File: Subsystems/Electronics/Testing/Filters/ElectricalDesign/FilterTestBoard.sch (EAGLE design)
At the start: 0 parts

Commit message: Created Schematic for Filter Test Board
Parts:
- added C1, C2, C3, C4: 1nF 10%, CougsInSpace-Capacitors:CAP-V-1NF-1608
- added C5, C6, C7, C8: 1nF 10%, CougsInSpace-Capacitors:CAP-H-1NF-1608
- added J1, J2: (no value), CougsInSpace-Connectors:COAX-BNC-T-R
- added R1, R2, R3, R4: 0Ω <20mΩ, CougsInSpace-Resistors:RES-H-0-1608
- added R5, R6, R7, R8: 0Ω <20mΩ, CougsInSpace-Resistors:RES-V-0-1608
- added SW1, SW2, SW3: (no value), CougsInSpace-Switches:SWITCH-DPDT-100DP1T1B1M2QE
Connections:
- new net N$1: C1.1, R1.2, R2.1
- new net N$10: C4.1, C7.1, R4.2
- new net N$11: R1.1, SW1.1-B
- new net N$12: C6.2, R6.2, SW3.1-A
- new net N$13: C5.2, C6.1, R5.2
- new net N$14: J1.CENTER, SW1.COM-A, SW2.COM-A, SW3.COM-A
- new net N$15: J2.CENTER, SW1.COM-B, SW2.COM-B, SW3.COM-B
- new net N$2: C2.1, R2.2, SW1.1-A
- new net N$3: C8.2, R8.2, SW2.1-A
- new net N$4: C5.1, SW3.1-B
- new net N$7: C7.2, C8.1, R7.2
- new net N$8: C3.1, R3.2, R4.1
- new net N$9: R3.1, SW2.1-B
- new net PGND: C1.2, C2.2, C3.2, C4.2, J1.SHIELD, J2.SHIELD, R5.1, R6.1, R7.1, R8.1
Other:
- note added: "Band Pass Filter"
- note added: "Connector: Input 50Ω"
- note added: "Connector: Output 1MΩ"
- note added: "High Pass Filter"
- note added: "Low Pass Filter"
- note added: "Page 1: Block Diagram Page 2: Filters, Connectors"
- note added: "Switch"
- note removed: "Connector: From Board"

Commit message: Laid out Board
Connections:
- net N$1 renamed LOW_INT
- net N$10 renamed BAND_INT1
- net N$11 renamed LOW_IN
- net N$12 renamed HIGH_OUT
- net N$13 renamed HIGH_INT
- net N$14 renamed INPUT
- net N$15 renamed OUTPUT
- net N$2 renamed LOW_OUT
- net N$3 renamed BAND_OUT
- net N$4 renamed HIGH_IN
- net N$7 renamed BAND_INT2
- net N$8 renamed BAND_INT0
- net N$9 renamed BAND_IN
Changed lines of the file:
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@@
 </attributes>
 <variantdefs>
+<variantdef name="EPS Test"/>
 </variantdefs>
 <classes>
@@
 </busses>
 <nets>
-<net name="N$1" class="0">
+<net name="LOW_INT" class="0">
 <segment>
 <pinref part="R1" gate="G$1" pin="2"/>
@@
 </segment>
 </net>
-<net name="N$2" class="0">
+<net name="LOW_OUT" class="0">
 <segment>
 <pinref part="R2" gate="G$1" pin="2"/>
@@
 </segment>
 </net>
-<net name="N$8" class="0">
+<net name="BAND_INT0" class="0">
 <segment>
 <pinref part="R3" gate="G$1" pin="2"/>
@@
 </segment>
 </net>
-<net name="N$12" class="0">
+<net name="HIGH_OUT" class="0">
 <segment>
 <pinref part="C6" gate="G$1" pin="2"/>
@@
 </segment>
 </net>
-<net name="N$13" class="0">
+<net name="HIGH_INT" class="0">
 <segment>
 <pinref part="C6" gate="G$1" pin="1"/>
@@
 </segment>
 </net>
-<net name="N$3" class="0">
+<net name="BAND_OUT" class="0">
 <segment>
 <pinref part="C8" gate="G$1" pin="2"/>
@@
 </segment>
 </net>
-<net name="N$7" class="0">
+<net name="BAND_INT2" class="0">
 <segment>
 <pinref part="C8" gate="G$1" pin="1"/>
@@
 </segment>
 </net>
-<net name="N$10" class="0">
+<net name="BAND_INT1" class="0">
 <segment>
 <pinref part="C7" gate="G$1" pin="1"/>
@@
 </segment>
 </net>
-<net name="N$4" class="0">
+<net name="HIGH_IN" class="0">
 <segment>
 <pinref part="C5" gate="G$1" pin="1"/>
@@
 </segment>
 </net>
-<net name="N$9" class="0">
+<net name="BAND_IN" class="0">
 <segment>
 <pinref part="R3" gate="G$1" pin="1"/>
@@
 </segment>
 </net>
-<net name="N$11" class="0">
+<net name="LOW_IN" class="0">
 <segment>
 <pinref part="R1" gate="G$1" pin="1"/>
@@
 </segment>
 </net>
-<net name="N$14" class="0">
+<net name="INPUT" class="0">
 <segment>
 <pinref part="J1" gate="G$1" pin="CENTER"/>
@@
 </segment>
 </net>
-<net name="N$15" class="0">
+<net name="OUTPUT" class="0">
 <segment>
 <pinref part="J2" gate="G$1" pin="CENTER"/>

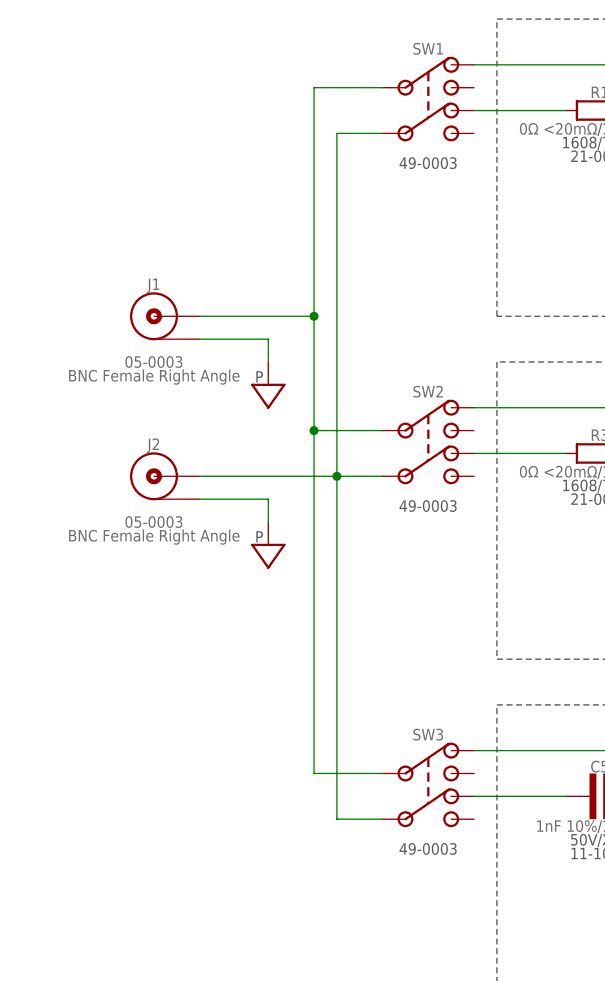
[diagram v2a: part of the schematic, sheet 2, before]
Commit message: Adjusted Board Layout
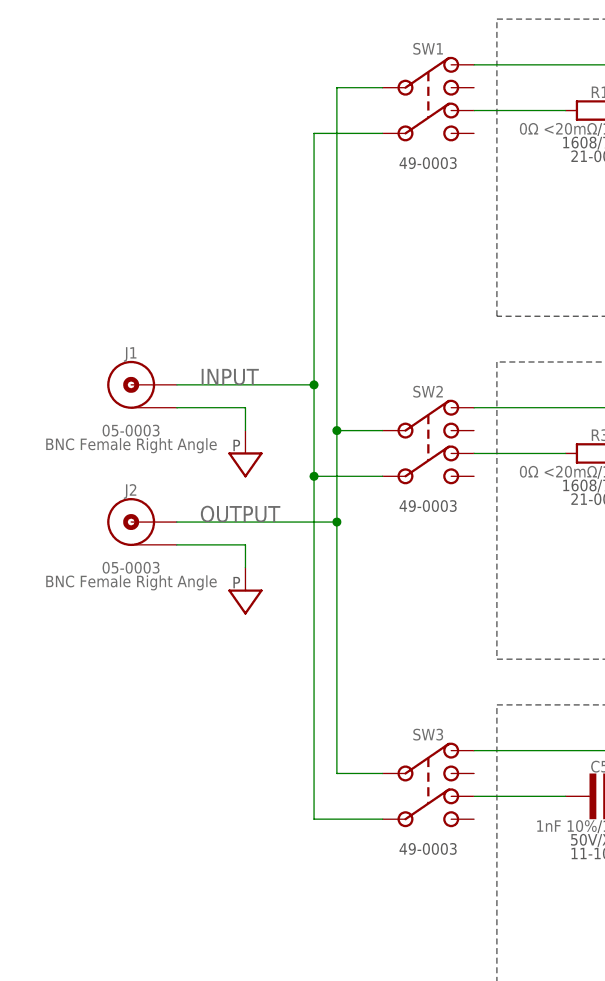
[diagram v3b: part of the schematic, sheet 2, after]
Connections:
- net INPUT: now also SW1.COM-B, SW2.COM-B, SW3.COM-B; no longer SW1.COM-A, SW2.COM-A, SW3.COM-A
- net OUTPUT: now also SW1.COM-A, SW2.COM-A, SW3.COM-A; no longer SW1.COM-B, SW2.COM-B, SW3.COM-B
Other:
- moved on the sheet: J1, J2
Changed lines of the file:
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@@
 <part name="SW2" library="CougsInSpace-Switches" deviceset="SWITCH-DPDT" device="-100DP1T1B1M2QE"/>
 <part name="SW3" library="CougsInSpace-Switches" deviceset="SWITCH-DPDT" device="-100DP1T1B1M2QE"/>
-<part name="R1" library="CougsInSpace-Resistors" deviceset="RES-H" device="-1608" technology="-0" value="0Ω &lt;20mΩ"/>
-<part name="R2" library="CougsInSpace-Resistors" deviceset="RES-H" device="-1608" technology="-0" value="0Ω &lt;20mΩ"/>
+<part name="R1" library="CougsInSpace-Resistors" deviceset="RES-H" device="-1608" technology="-0" value="0Ω &lt;20mΩ">
+<variant name="EPS Test" technology="-158K" value="158kΩ 0.1%"/>
+</part>
+<part name="R2" library="CougsInSpace-Resistors" deviceset="RES-H" device="-1608" technology="-0" value="0Ω &lt;20mΩ">
+<variant name="EPS Test" technology="-158K" value="158kΩ 0.1%"/>
+</part>
 <part name="C1" library="CougsInSpace-Capacitors" deviceset="CAP-V" device="-1608" technology="-1NF" value="1nF 10%"/>
 <part name="C2" library="CougsInSpace-Capacitors" deviceset="CAP-V" device="-1608" technology="-1NF" value="1nF 10%"/>
 <part name="J2" library="CougsInSpace-Connectors" deviceset="COAX" device="-BNC-T-R"/>
-<part name="R3" library="CougsInSpace-Resistors" deviceset="RES-H" device="-1608" technology="-0" value="0Ω &lt;20mΩ"/>
-<part name="R4" library="CougsInSpace-Resistors" deviceset="RES-H" device="-1608" technology="-0" value="0Ω &lt;20mΩ"/>
+<part name="R3" library="CougsInSpace-Resistors" deviceset="RES-H" device="-1608" technology="-0" value="0Ω &lt;20mΩ">
+<variant name="EPS Test" technology="-158K" value="158kΩ 0.1%"/>
+</part>
+<part name="R4" library="CougsInSpace-Resistors" deviceset="RES-H" device="-1608" technology="-0" value="0Ω &lt;20mΩ">
+<variant name="EPS Test" technology="-158K" value="158kΩ 0.1%"/>
+</part>
 <part name="C3" library="CougsInSpace-Capacitors" deviceset="CAP-V" device="-1608" technology="-1NF" value="1nF 10%"/>
 <part name="C4" library="CougsInSpace-Capacitors" deviceset="CAP-V" device="-1608" technology="-1NF" value="1nF 10%"/>
@@
 <attribute name="TITLE" x="227.33" y="20.32" size="3.81" layer="94" ratio="15" align="bottom-right"/>
 </instance>
-<instance part="J1" gate="G$1" x="50.8" y="121.92" smashed="yes" rot="MR0">
-<attribute name="NAME" x="50.8" y="125.476" size="1.27" layer="95" rot="MR0" align="center"/>
-<attribute name="VALUE" x="50.8" y="118.364" size="1.27" layer="96" rot="MR0" align="center"/>
-<attribute name="SKU" x="50.8" y="116.84" size="1.27" layer="96" rot="MR0" align="center"/>
-<attribute name="PACKAGE" x="50.8" y="115.316" size="1.27" layer="96" rot="MR0" align="center"/>
+<instance part="J1" gate="G$1" x="48.26" y="114.3" smashed="yes" rot="MR0">
+<attribute name="NAME" x="48.26" y="117.856" size="1.27" layer="95" rot="MR0" align="center"/>
+<attribute name="VALUE" x="48.26" y="110.744" size="1.27" layer="96" rot="MR0" align="center"/>
+<attribute name="SKU" x="48.26" y="109.22" size="1.27" layer="96" rot="MR0" align="center"/>
+<attribute name="PACKAGE" x="48.26" y="107.696" size="1.27" layer="96" rot="MR0" align="center"/>
 </instance>
 <instance part="SW1" gate="G$1" x="81.28" y="144.78" smashed="yes">
@@
 <attribute name="TEMP" x="142.494" y="132.08" size="1.27" layer="97" align="center-left"/>
 </instance>
-<instance part="J2" gate="G$1" x="50.8" y="104.14" smashed="yes" rot="MR0">
-<attribute name="NAME" x="50.8" y="107.696" size="1.27" layer="95" rot="MR0" align="center"/>
-<attribute name="VALUE" x="50.8" y="100.584" size="1.27" layer="96" rot="MR0" align="center"/>
-<attribute name="SKU" x="50.8" y="99.06" size="1.27" layer="96" rot="MR0" align="center"/>
-<attribute name="PACKAGE" x="50.8" y="97.536" size="1.27" layer="96" rot="MR0" align="center"/>
+<instance part="J2" gate="G$1" x="48.26" y="99.06" smashed="yes" rot="MR0">
+<attribute name="NAME" x="48.26" y="102.616" size="1.27" layer="95" rot="MR0" align="center"/>
+<attribute name="VALUE" x="48.26" y="95.504" size="1.27" layer="96" rot="MR0" align="center"/>
+<attribute name="SKU" x="48.26" y="93.98" size="1.27" layer="96" rot="MR0" align="center"/>
+<attribute name="PACKAGE" x="48.26" y="92.456" size="1.27" layer="96" rot="MR0" align="center"/>
 </instance>
 <instance part="R3" gate="G$1" x="101.6" y="106.68" smashed="yes">
@@
 <attribute name="SKU" x="140.97" y="60.452" size="1.27" layer="97" align="center-left"/>
 </instance>
-<instance part="SUPPLY1" gate="G$1" x="63.5" y="114.3" smashed="yes"/>
-<instance part="SUPPLY2" gate="G$1" x="63.5" y="96.52" smashed="yes"/>
+<instance part="SUPPLY1" gate="G$1" x="60.96" y="106.68" smashed="yes"/>
+<instance part="SUPPLY2" gate="G$1" x="60.96" y="91.44" smashed="yes"/>
 <instance part="SUPPLY3" gate="G$1" x="139.7" y="127" smashed="yes"/>
 <instance part="SUPPLY4" gate="G$1" x="111.76" y="127" smashed="yes"/>
@@
 <segment>
 <pinref part="J1" gate="G$1" pin="SHIELD"/>
-<wire x1="55.88" y1="119.38" x2="63.5" y2="119.38" width="0.1524" layer="91"/>
+<wire x1="53.34" y1="111.76" x2="60.96" y2="111.76" width="0.1524" layer="91"/>
 <pinref part="SUPPLY1" gate="G$1" pin="PGND"/>
-<wire x1="63.5" y1="119.38" x2="63.5" y2="116.84" width="0.1524" layer="91"/>
+<wire x1="60.96" y1="111.76" x2="60.96" y2="109.22" width="0.1524" layer="91"/>
 </segment>
 <segment>
 <pinref part="J2" gate="G$1" pin="SHIELD"/>
-<wire x1="63.5" y1="101.6" x2="55.88" y2="101.6" width="0.1524" layer="91"/>
+<wire x1="60.96" y1="96.52" x2="53.34" y2="96.52" width="0.1524" layer="91"/>
 <pinref part="SUPPLY2" gate="G$1" pin="PGND"/>
-<wire x1="63.5" y1="99.06" x2="63.5" y2="101.6" width="0.1524" layer="91"/>
+<wire x1="60.96" y1="93.98" x2="60.96" y2="96.52" width="0.1524" layer="91"/>
 </segment>
 <segment>
@@
 <segment>
 <pinref part="J1" gate="G$1" pin="CENTER"/>
-<wire x1="55.88" y1="121.92" x2="68.58" y2="121.92" width="0.1524" layer="91"/>
-<wire x1="68.58" y1="121.92" x2="68.58" y2="147.32" width="0.1524" layer="91"/>
+<wire x1="53.34" y1="114.3" x2="68.58" y2="114.3" width="0.1524" layer="91"/>
+<wire x1="68.58" y1="114.3" x2="68.58" y2="142.24" width="0.1524" layer="91"/>
+<junction x="68.58" y="114.3"/>
+<wire x1="68.58" y1="114.3" x2="68.58" y2="104.14" width="0.1524" layer="91"/>
+<pinref part="SW3" gate="G$1" pin="COM-B"/>
+<wire x1="68.58" y1="104.14" x2="68.58" y2="66.04" width="0.1524" layer="91"/>
+<wire x1="68.58" y1="66.04" x2="76.2" y2="66.04" width="0.1524" layer="91"/>
+<pinref part="SW2" gate="G$1" pin="COM-B"/>
+<wire x1="76.2" y1="104.14" x2="68.58" y2="104.14" width="0.1524" layer="91"/>
+<junction x="68.58" y="104.14"/>
+<pinref part="SW1" gate="G$1" pin="COM-B"/>
+<wire x1="76.2" y1="142.24" x2="68.58" y2="142.24" width="0.1524" layer="91"/>
+<label x="55.88" y="114.3" size="1.778" layer="95"/>
+</segment>
+</net>
+<net name="OUTPUT" class="0">
+<segment>
+<wire x1="71.12" y1="109.22" x2="71.12" y2="99.06" width="0.1524" layer="91"/>
+<junction x="71.12" y="109.22"/>
+<wire x1="71.12" y1="99.06" x2="71.12" y2="71.12" width="0.1524" layer="91"/>
+<wire x1="71.12" y1="109.22" x2="71.12" y2="147.32" width="0.1524" layer="91"/>
+<pinref part="SW3" gate="G$1" pin="COM-A"/>
+<wire x1="76.2" y1="71.12" x2="71.12" y2="71.12" width="0.1524" layer="91"/>
+<pinref part="SW2" gate="G$1" pin="COM-A"/>
+<wire x1="76.2" y1="109.22" x2="71.12" y2="109.22" width="0.1524" layer="91"/>
 <pinref part="SW1" gate="G$1" pin="COM-A"/>
-<wire x1="68.58" y1="147.32" x2="76.2" y2="147.32" width="0.1524" layer="91"/>
-<wire x1="68.58" y1="121.92" x2="68.58" y2="109.22" width="0.1524" layer="91"/>
-<junction x="68.58" y="121.92"/>
-<pinref part="SW2" gate="G$1" pin="COM-A"/>
-<wire x1="68.58" y1="109.22" x2="76.2" y2="109.22" width="0.1524" layer="91"/>
-<wire x1="68.58" y1="109.22" x2="68.58" y2="71.12" width="0.1524" layer="91"/>
-<junction x="68.58" y="109.22"/>
-<pinref part="SW3" gate="G$1" pin="COM-A"/>
-<wire x1="68.58" y1="71.12" x2="76.2" y2="71.12" width="0.1524" layer="91"/>
-</segment>
-</net>
-<net name="OUTPUT" class="0">
-<segment>
+<wire x1="71.12" y1="147.32" x2="76.2" y2="147.32" width="0.1524" layer="91"/>
 <pinref part="J2" gate="G$1" pin="CENTER"/>
-<pinref part="SW2" gate="G$1" pin="COM-B"/>
-<wire x1="55.88" y1="104.14" x2="71.12" y2="104.14" width="0.1524" layer="91"/>
-<pinref part="SW3" gate="G$1" pin="COM-B"/>
-<wire x1="71.12" y1="104.14" x2="76.2" y2="104.14" width="0.1524" layer="91"/>
-<wire x1="71.12" y1="104.14" x2="71.12" y2="66.04" width="0.1524" layer="91"/>
-<wire x1="71.12" y1="66.04" x2="76.2" y2="66.04" width="0.1524" layer="91"/>
-<junction x="71.12" y="104.14"/>
-<wire x1="71.12" y1="104.14" x2="71.12" y2="142.24" width="0.1524" layer="91"/>
-<pinref part="SW1" gate="G$1" pin="COM-B"/>
-<wire x1="71.12" y1="142.24" x2="76.2" y2="142.24" width="0.1524" layer="91"/>
-</segment>
-</net>
+<wire x1="53.34" y1="99.06" x2="71.12" y2="99.06" width="0.1524" layer="91"/>
+<junction x="71.12" y="99.06"/>
+<label x="55.88" y="99.06" size="1.778" layer="95"/>
+</segment>
+</net>
